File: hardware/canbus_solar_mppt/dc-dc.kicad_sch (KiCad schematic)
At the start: 59 parts, among them J1 SOLAR_IN, J2 BATT2, J3 BATT1, Q1 SIR164ADP, Q2 SIR164ADP, Q3 SiSS27DN, Q4 SiSS27DN, Q5 SiSS27DN, Q6 SiSS27DN, U2 LP4951C, U3 NCP5901B, U4 PAC1953-1, U5 DGD0215, U6 DGD0215

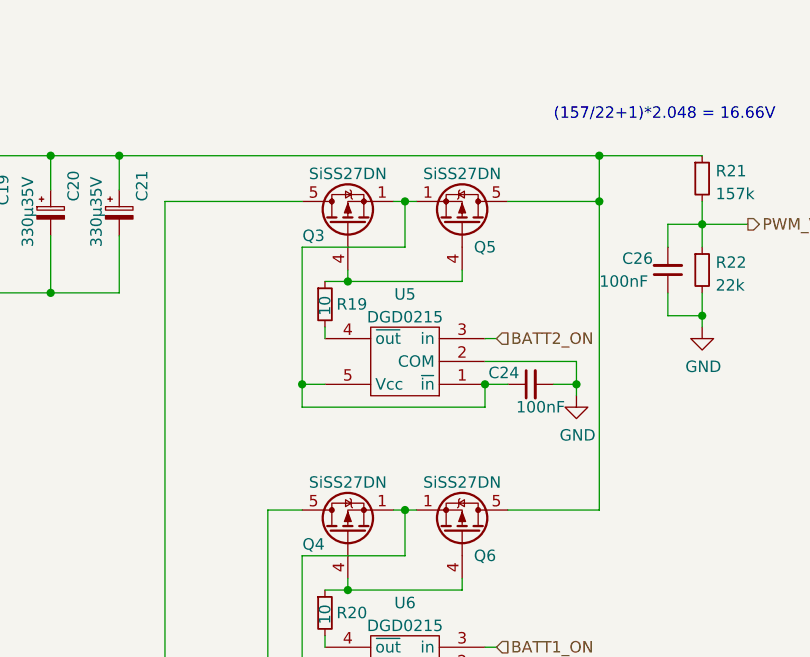
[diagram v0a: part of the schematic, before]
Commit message: Change Pmos transistors for a reference with larger package. Ajust some other footprints.
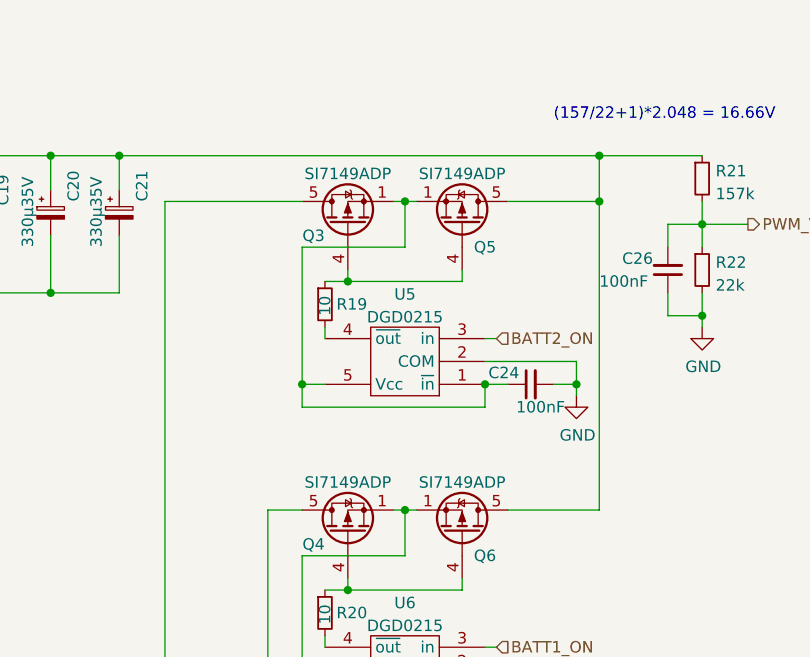
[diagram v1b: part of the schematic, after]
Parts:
- C24, C25: footprint Capacitor_SMD:C_1206_3216Metric_Pad1.33x1.80mm_HandSolder -> Capacitor_SMD:C_0603_1608Metric_Pad1.08x0.95mm_HandSolder
- Q3, Q4, Q5, Q6: value SiSS27DN -> SI7149ADP; footprint Package_SO:Vishay_PowerPAK_1212-8_Single -> Package_SO:PowerPAK_SO-8_Single; P/N (none) -> SI7149ADP-T1-GE3
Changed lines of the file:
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@@
     (in_bom yes) (on_board yes)
     (property "Reference" "Q3" (id 0) (at 226.06 67.31 90))
-    (property "Value" "SiSS27DN" (id 1) (at 229.87 60.4321 90))
-    (property "Footprint" "Package_SO:Vishay_PowerPAK_1212-8_Single" (id 2) (at 231.775 60.96 0)
+    (property "Value" " SI7149ADP" (id 1) (at 229.87 60.4321 90))
+    (property "Footprint" "Package_SO:PowerPAK_SO-8_Single" (id 2) (at 231.775 60.96 0)
       (effects (font (size 1.27 1.27) italic) (justify left) hide)
     )
     (property "Datasheet" "http://www.vishay.com/docs/62847/siss27dn.pdf" (id 3) (at 229.87 66.04 90)
       (effects (font (size 1.27 1.27)) (justify left) hide)
+    )
+    (property "P/N" " SI7149ADP-T1-GE3 " (id 4) (at 229.87 66.04 0)
+      (effects (font (size 1.27 1.27)) hide)
     )
     (pin "1")
@@
       (effects (font (size 1.27 1.27)) (justify left))
     )
-    (property "Footprint" "Capacitor_SMD:C_1206_3216Metric_Pad1.33x1.80mm_HandSolder" (id 2) (at 250.19 118.11 0)
+    (property "Footprint" "Capacitor_SMD:C_0603_1608Metric_Pad1.08x0.95mm_HandSolder" (id 2) (at 250.19 118.11 0)
       (effects (font (size 1.27 1.27)) hide)
     )
@@
     (in_bom yes) (on_board yes)
     (property "Reference" "Q4" (id 0) (at 226.06 101.6 90))
-    (property "Value" "SiSS27DN" (id 1) (at 229.87 94.7221 90))
-    (property "Footprint" "Package_SO:Vishay_PowerPAK_1212-8_Single" (id 2) (at 231.775 95.25 0)
+    (property "Value" " SI7149ADP" (id 1) (at 229.87 94.7221 90))
+    (property "Footprint" "Package_SO:PowerPAK_SO-8_Single" (id 2) (at 231.775 95.25 0)
       (effects (font (size 1.27 1.27) italic) (justify left) hide)
     )
-    (property "Datasheet" "http://www.vishay.com/docs/62847/siss27dn.pdf" (id 3) (at 229.87 100.33 90)
-      (effects (font (size 1.27 1.27)) (justify left) hide)
+    (property "Datasheet" "" (id 3) (at 229.87 100.33 90)
+      (effects (font (size 1.27 1.27)) (justify left) hide)
+    )
+    (property "P/N" " SI7149ADP-T1-GE3 " (id 4) (at 229.87 100.33 0)
+      (effects (font (size 1.27 1.27)) hide)
     )
     (pin "1")
@@
     (in_bom yes) (on_board yes)
     (property "Reference" "Q6" (id 0) (at 245.11 102.87 90))
-    (property "Value" "SiSS27DN" (id 1) (at 242.57 94.7221 90))
-    (property "Footprint" "Package_SO:Vishay_PowerPAK_1212-8_Single" (id 2) (at 240.665 95.25 0)
+    (property "Value" " SI7149ADP" (id 1) (at 242.57 94.7221 90))
+    (property "Footprint" "Package_SO:PowerPAK_SO-8_Single" (id 2) (at 240.665 95.25 0)
       (effects (font (size 1.27 1.27) italic) (justify left) hide)
     )
-    (property "Datasheet" "http://www.vishay.com/docs/62847/siss27dn.pdf" (id 3) (at 242.57 100.33 90)
-      (effects (font (size 1.27 1.27)) (justify left) hide)
+    (property "Datasheet" "http://www.vishay.com/docs/62847/siss27dn.pd" (id 3) (at 242.57 100.33 90)
+      (effects (font (size 1.27 1.27)) (justify left) hide)
+    )
+    (property "P/N" " SI7149ADP-T1-GE3 " (id 4) (at 242.57 100.33 0)
+      (effects (font (size 1.27 1.27)) hide)
     )
     (pin "1")
@@
       (effects (font (size 1.27 1.27)) (justify left))
     )
-    (property "Footprint" "Capacitor_SMD:C_1206_3216Metric_Pad1.33x1.80mm_HandSolder" (id 2) (at 250.19 83.82 0)
+    (property "Footprint" "Capacitor_SMD:C_0603_1608Metric_Pad1.08x0.95mm_HandSolder" (id 2) (at 250.19 83.82 0)
       (effects (font (size 1.27 1.27)) hide)
     )
@@
     (in_bom yes) (on_board yes)
     (property "Reference" "Q5" (id 0) (at 245.11 68.58 90))
-    (property "Value" "SiSS27DN" (id 1) (at 242.57 60.4321 90))
-    (property "Footprint" "Package_SO:Vishay_PowerPAK_1212-8_Single" (id 2) (at 240.665 60.96 0)
+    (property "Value" " SI7149ADP" (id 1) (at 242.57 60.4321 90))
+    (property "Footprint" "Package_SO:PowerPAK_SO-8_Single" (id 2) (at 240.665 60.96 0)
       (effects (font (size 1.27 1.27) italic) (justify left) hide)
     )
-    (property "Datasheet" "http://www.vishay.com/docs/62847/siss27dn.pdf" (id 3) (at 242.57 66.04 90)
-      (effects (font (size 1.27 1.27)) (justify left) hide)
-    )
-    (pin "1")
+    (property "Datasheet" "" (id 3) (at 242.57 66.04 90)
+      (effects (font (size 1.27 1.27)) (justify left) hide)
+    )
+    (property "P/N" " SI7149ADP-T1-GE3 " (id 4) (at 242.57 66.04 0)
+      (effects (font (size 1.27 1.27)) hide)
+    )
+    (pin "1")
